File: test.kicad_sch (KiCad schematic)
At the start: 15 parts, among them U1 ATmega8L-8P, U2 74AHC595, U3 74AHC595, U4 74AHC595, U5 74AHC595, Y1 8 MHz Crystal

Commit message: add some more stuff
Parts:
- added Q1, Q10, Q11, Q12, Q13, Q14, Q15, Q16, Q2, Q3, Q4, Q5, Q6, Q7, Q8, Q9: MMBTA42, Package_TO_SOT_SMD:SOT-23W_Handsoldering, symbol Transistor_BJT:MMBTA42
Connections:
- net GNDREF: now also Q1.2 (E), Q10.2 (E), Q11.2 (E), Q12.2 (E), Q13.2 (E), Q14.2 (E), Q15.2 (E), Q16.2 (E), Q2.2 (E), Q3.2 (E), Q4.2 (E), Q5.2 (E), Q6.2 (E), Q7.2 (E), Q8.2 (E), Q9.2 (E)
- net at U2.1 (QB): now also Q2.1 (B)
- net at U2.15 (QA): now also Q1.1 (B)
- net at U2.2 (QC): now also Q3.1 (B)
- net at U2.3 (QD): now also Q4.1 (B)
- net at U2.4 (QE): now also Q5.1 (B)
- net at U2.5 (QF): now also Q6.1 (B)
- net at U2.6 (QG): now also Q7.1 (B)
- net at U2.7 (QH): now also Q8.1 (B)
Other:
- note added: "4.7k resistors here"
- moved on the sheet: C1, C2, C3, C4, C5, C6, C7, C8, C9, U1, U2, U3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

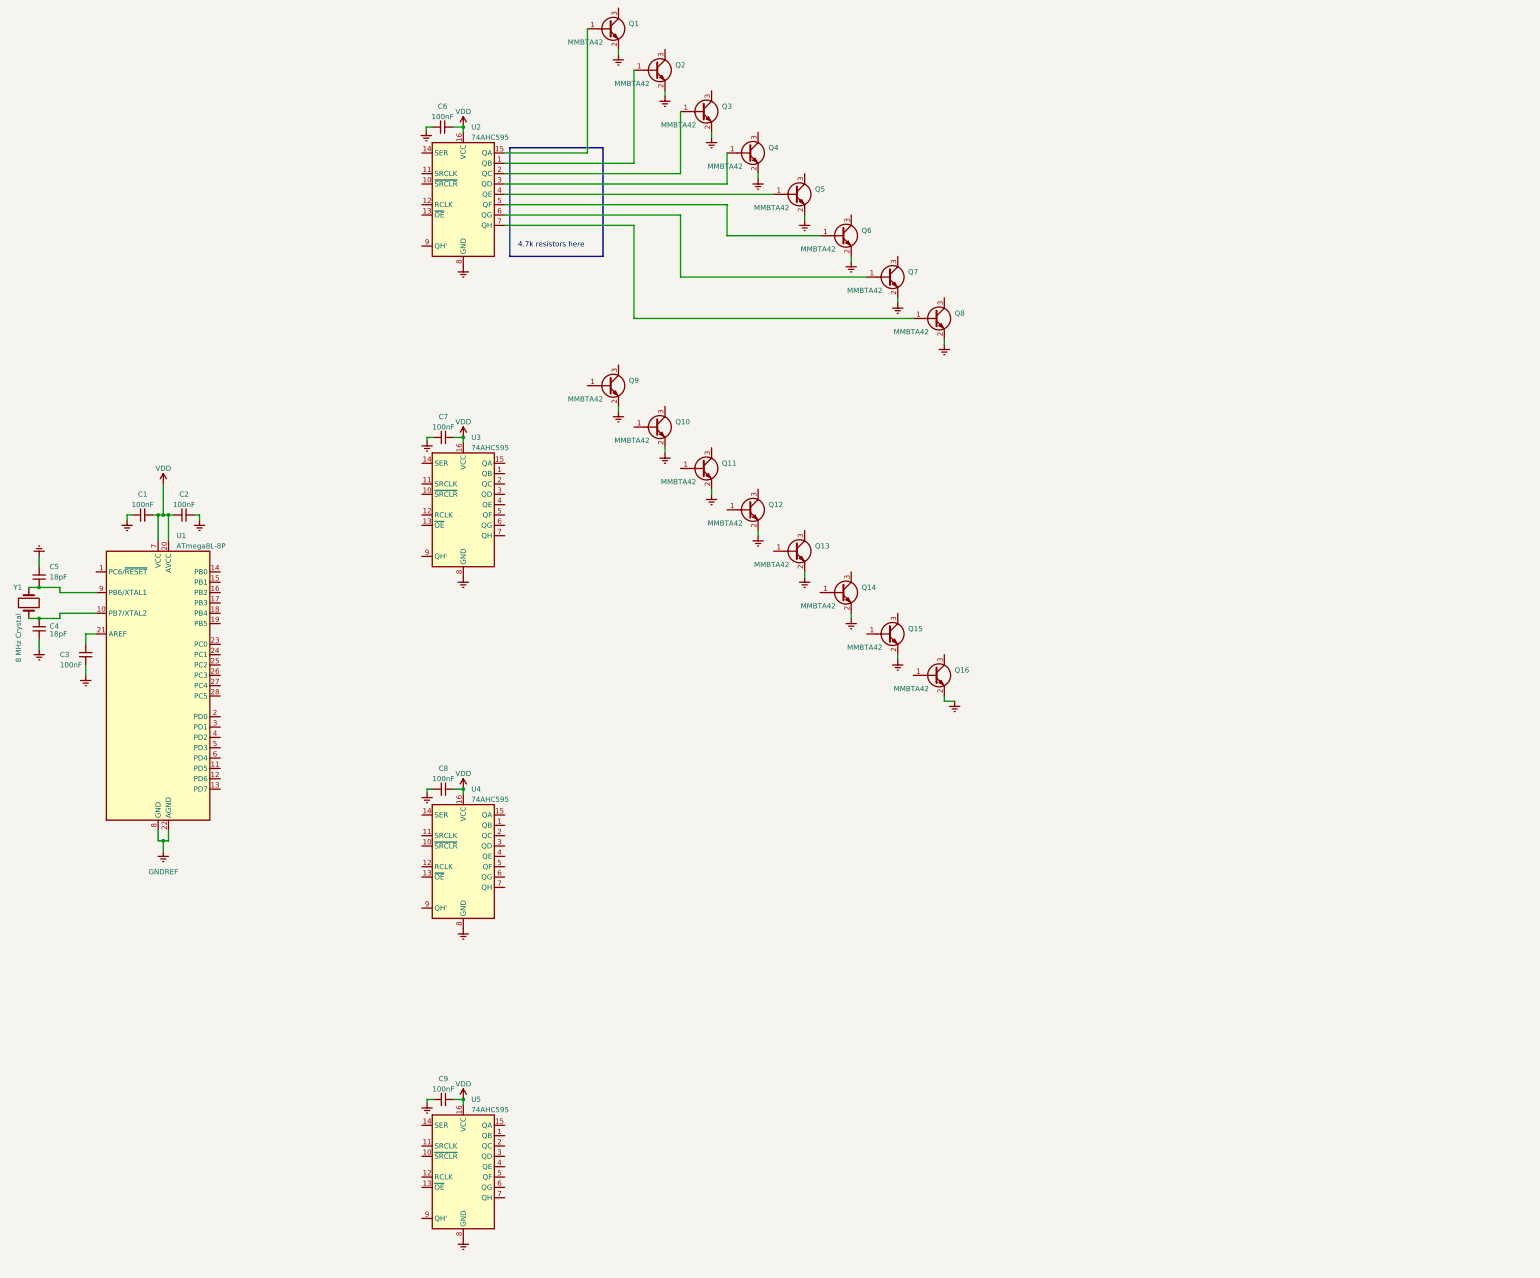
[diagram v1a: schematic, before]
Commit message: made most things smd
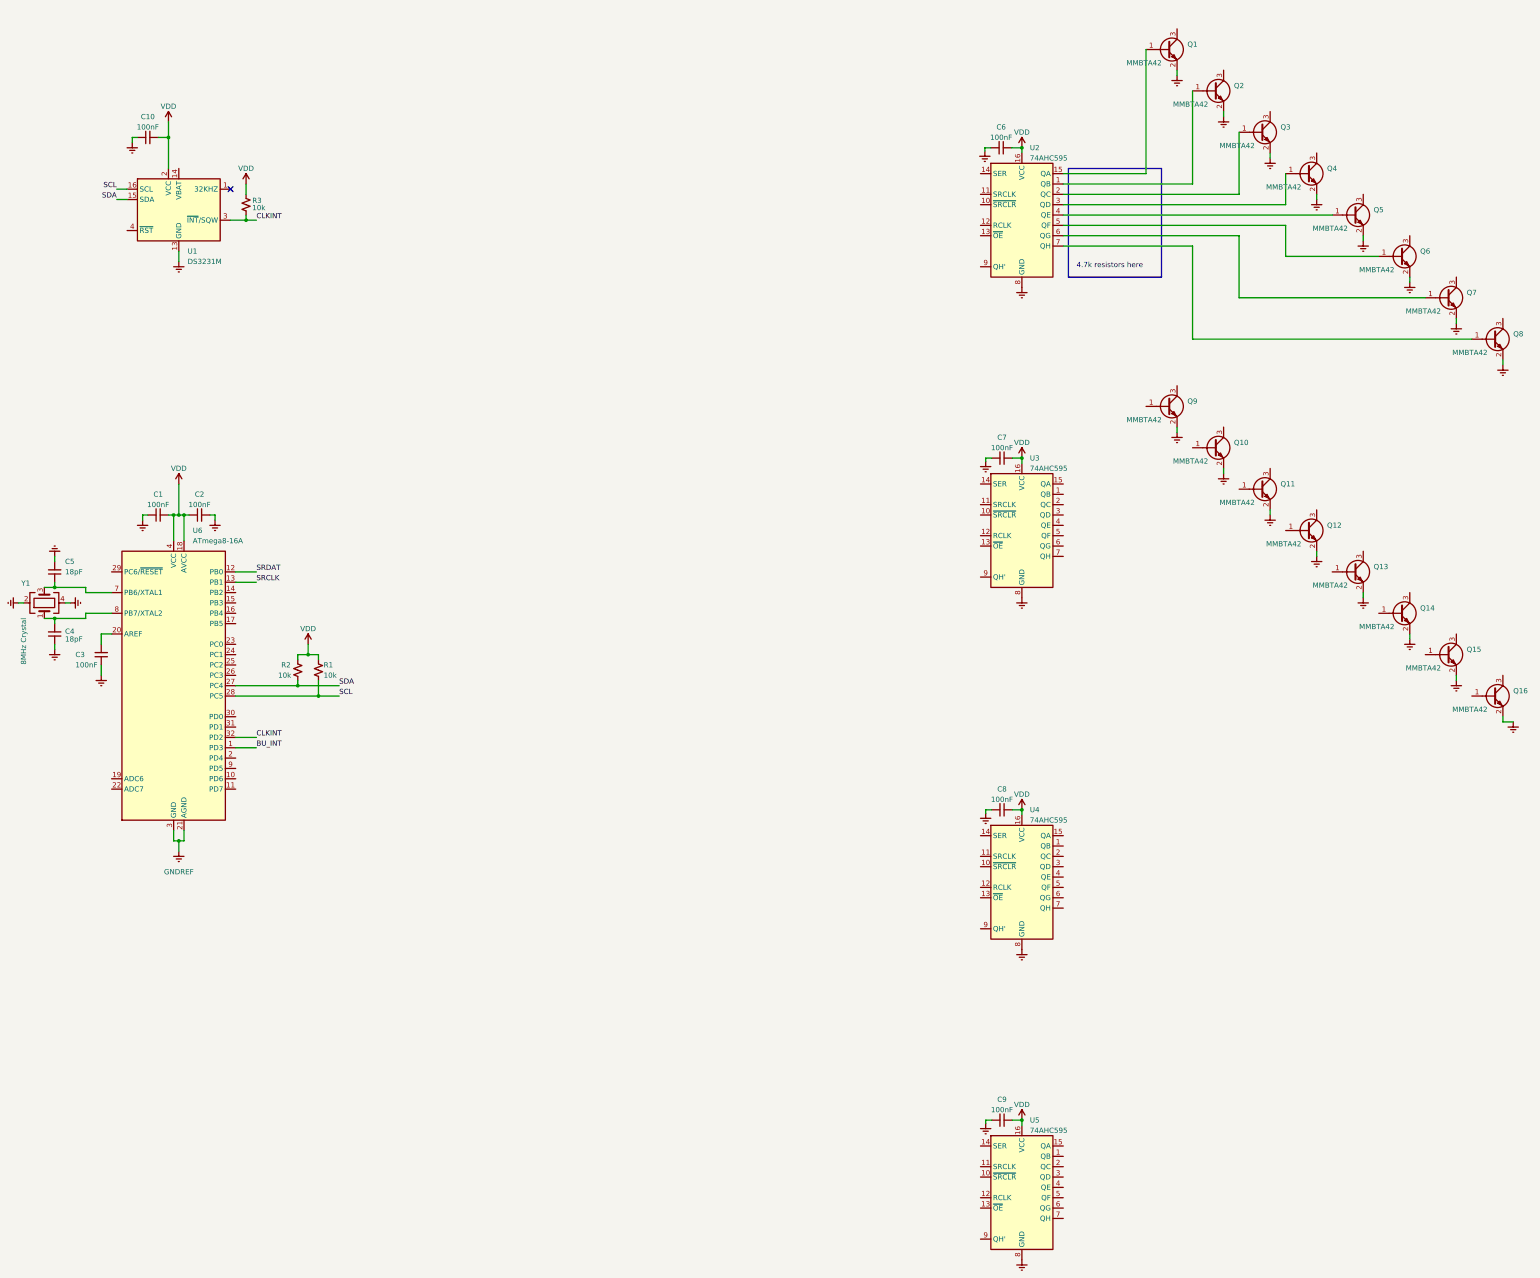
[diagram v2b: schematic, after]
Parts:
- removed U1: ATmega8L-8P, Package_DIP:DIP-28_W7.62mm, symbol MCU_Microchip_ATmega:ATmega8L-8P
- removed Y1: 8 MHz Crystal, Crystal:Crystal_HC49-U_Horizontal, symbol Device:Crystal
- added C10: 100nF, symbol Device:C_Small
- added R1, R2, R3: 10k, symbol Device:R_Small_US
- added U1: DS3231M, Package_SO:SOIC-16W_7.5x10.3mm_P1.27mm, symbol Timer_RTC:DS3231M
- added U6: ATmega8-16A, Package_QFP:TQFP-32_7x7mm_P0.8mm, symbol MCU_Microchip_ATmega:ATmega8-16A
- added Y1: 8MHz Crystal, Crystal:Crystal_SMD_0603-4Pin_6.0x3.5mm_HandSoldering, symbol Device:Crystal_GND24
- U2, U3, U4, U5: footprint Package_DIP:DIP-16_W7.62mm -> Package_SO:SOIC-16_3.9x9.9mm_P1.27mm
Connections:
- net GNDREF: now also C10.1, U1.10 (GND), U1.11 (GND), U1.12 (GND), U1.13 (GND), U1.5 (GND), U1.6 (GND), U1.7 (GND), U1.8 (GND), U1.9 (GND), U6.21 (AGND), U6.3 (GND), U6.5 (GND), Y1.2, Y1.4
- net VDD: now also C10.2, R1.1, R2.1, R3.1, U1.2 (VCC), U6.18 (AVCC), U6.4 (VCC), U6.6 (VCC)
- net at C5.1: now also U6.7 (PB6/XTAL1), Y1.3
- net at C4.2: now also U6.8 (PB7/XTAL2), Y1.1
- net at C3.2: now also U6.20 (AREF)
- new net BU_INT: U6.1 (PD3)
- new net CLKINT: R3.2, U1.3 (~{INT}/SQW), U6.32 (PD2)
- new net SCL: R1.2, U1.16 (SCL), U6.28 (PC5)
- new net SDA: R2.2, U1.15 (SDA), U6.27 (PC4)
- new net SRCLK: U6.13 (PB1)
- new net SRDAT: U6.12 (PB0)
- no-connect marks 0 -> 1
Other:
- moved on the sheet: C1, C2, C3, C4, C5, C6, C7, C8, C9, Q1, Q10, Q11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

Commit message: eod commit
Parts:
- added C11: 100nF, symbol Device:C_Small
- added Q17, Q18, Q19, Q20, Q21, Q22, Q23, Q24, Q25, Q26, Q27, Q28, Q29, Q30, Q31, Q32, Q33, Q34, Q35, Q36, Q37, Q38, Q39, Q40: MMBTA42, Package_TO_SOT_SMD:SOT-23W_Handsoldering, symbol Transistor_BJT:MMBTA42
- added R10, R11, R12, R13, R14, R15, R16, R17, R18, R19, R20, R21, R22, R23, R24, R25, R26, R27, R28, R29, R30, R31, R32, R33, R34, R35, R36, R37, R38, R39, R4, R40, R41, R42, R43, R5, R6, R7, R8, R9: 4.7k, symbol Device:R_Small_US
- added U7: 74AHC595, Package_SO:SOIC-16_3.9x9.9mm_P1.27mm, symbol 74xx:74AHC595
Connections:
- net GNDREF: now also C11.2, Q17.2 (E), Q18.2 (E), Q19.2 (E), Q20.2 (E), Q21.2 (E), Q22.2 (E), Q23.2 (E), Q24.2 (E), Q25.2 (E), Q26.2 (E), Q27.2 (E), Q28.2 (E), Q29.2 (E), Q30.2 (E), Q31.2 (E), Q32.2 (E), Q33.2 (E), Q34.2 (E), Q35.2 (E), Q36.2 (E), Q37.2 (E), Q38.2 (E), Q39.2 (E), Q40.2 (E), U7.8 (GND)
- net VDD: now also C11.1, U7.16 (VCC)
- net at Q9.1 (B): now also R12.2
- net at Q15.1 (B): now also R18.2
- net at Q5.1 (B): now also R8.2; no longer U2.4 (QE)
- net at U2.6 (QG): now also R10.1; no longer Q7.1 (B)
- net at Q13.1 (B): now also R16.2
- net at Q11.1 (B): now also R14.2
- net at Q10.1 (B): now also R13.2
- net at Q6.1 (B): now also R9.2; no longer U2.5 (QF)
- net at Q16.1 (B): now also R19.2
- net at Q3.1 (B): now also R6.2; no longer U2.2 (QC)
- net at U5.1 (QB): now also R29.1
- net at U5.15 (QA): now also R28.1
- net at U5.2 (QC): now also R30.1
- net at U5.3 (QD): now also R31.1
- net at U5.4 (QE): now also R32.1
- net at U5.5 (QF): now also R33.1
- net at U5.6 (QG): now also R34.1
- net at U5.7 (QH): now also R35.1
- net at Q2.1 (B): now also R5.2; no longer U2.1 (QB)
- net at Q4.1 (B): now also R7.2; no longer U2.3 (QD)
- net at Q12.1 (B): now also R15.2
- net at Q1.1 (B): now also R4.2; no longer U2.15 (QA)
- net at U2.7 (QH): now also R11.1; no longer Q8.1 (B)
- net at U3.1 (QB): now also R13.1
- net at U3.15 (QA): now also R12.1
- net at U3.2 (QC): now also R14.1
- net at U3.3 (QD): now also R15.1
- net at U3.4 (QE): now also R16.1
- net at U3.5 (QF): now also R17.1
- net at U3.6 (QG): now also R18.1
- net at U3.7 (QH): now also R19.1
- net at Q14.1 (B): now also R17.2
- net at U4.1 (QB): now also R21.1
- net at U4.15 (QA): now also R20.1
- net at U4.2 (QC): now also R22.1
- net at U4.3 (QD): now also R23.1
- net at U4.4 (QE): now also R24.1
- net at U4.5 (QF): now also R25.1
- net at U4.6 (QG): now also R26.1
- net at U4.7 (QH): now also R27.1
- new net: R43.1, U7.7 (QH)
- new net: Q40.1 (B), R43.2
- new net: Q33.1 (B), R36.2
- new net: Q23.1 (B), R26.2
- new net: Q21.1 (B), R24.2
- new net: Q19.1 (B), R22.2
- new net: Q22.1 (B), R25.2
- new net: Q20.1 (B), R23.2
- new net: Q24.1 (B), R27.2
- new net: Q26.1 (B), R29.2
- new net: Q7.1 (B), R10.2
- new net: R40.1, U7.4 (QE)
- new net: Q37.1 (B), R40.2
- new net: Q8.1 (B), R11.2
- new net: Q34.1 (B), R37.2
- new net: Q32.1 (B), R35.2
- new net: Q30.1 (B), R33.2
- new net: Q17.1 (B), R20.2
- new net: Q27.1 (B), R30.2
- new net: R39.1, U7.3 (QD)
- new net: Q36.1 (B), R39.2
- new net: R36.1, U7.15 (QA)
- new net: Q31.1 (B), R34.2
- new net: Q29.1 (B), R32.2
- new net: R42.1, U7.6 (QG)
- new net: Q39.1 (B), R42.2
- new net: R9.1, U2.5 (QF)
- new net: R37.1, U7.1 (QB)
- new net: R38.1, U7.2 (QC)
- new net: R41.1, U7.5 (QF)
- new net: Q25.1 (B), R28.2
- new net: Q18.1 (B), R21.2
- new net: R8.1, U2.4 (QE)
- new net: Q38.1 (B), R41.2
- new net: Q35.1 (B), R38.2
- new net: R4.1, U2.15 (QA)
- new net: R5.1, U2.1 (QB)
- new net: R7.1, U2.3 (QD)
- new net: R6.1, U2.2 (QC)
- new net: Q28.1 (B), R31.2
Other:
- note added: "27k 0.5W Anode Resistors 2512 Package"
- note removed: "4.7k resistors here"
- moved on the sheet: C10, C6, Q1, Q2, Q3, Q4, Q5, Q6, Q7, Q8, R1, R2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
